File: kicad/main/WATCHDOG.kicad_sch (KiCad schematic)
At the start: 3 parts, among them U2 TPS3828-33DBVR

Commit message: Second review round
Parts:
- removed R135: 100k, Resistor_SMD:R_0603_1608Metric, symbol Device:R_US
- removed U2: TPS3828-33DBVR, JLCImport:TPS3828-33DBVR, symbol JLCImport:TPS3828-33DBVR
- added U3: STWD100NYWY3F, JLCImport:STWD100NYWY3F, symbol JLCImport:STWD100NYWY3F
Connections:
- net GND: now also U3.2 (GND)
- net VCC-3V3-P: now also U3.5 (VCC)
- net WDI: now also U3.4 (WDI)
- net ~{PULSE_OUT}: now also U3.1 (WDO)
- new net ~{EN}: U3.3 (EN)

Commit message: STM32 power rail switch
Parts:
- C56: value 100nF/50V -> 100nF/6.3V; LCSC C1591 -> C5356672
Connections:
- net VCC-3V3-P renamed VCC-3V3
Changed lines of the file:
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@@
 	(generator_version "10.0")
 	(paper "A2")
-	(junction
-		(at 271.78 194.31)
-		(diameter 0)
-		(color 0 0 0 0)
-	)
 	(wire
 		(pts
@@
 			(width 0)
 			(type default)
+		)
+	)
+	(global_label "VCC-3V3"
+		(shape input)
+		(at 271.78 194.31 90)
+		(fields_autoplaced yes)
+		(effects
+			(font
+				(size 1.27 1.27)
+			)
+			(justify left)
+		)
+		(property "Intersheetrefs" "${INTERSHEET_REFS}"
+			(at 271.78 182.6162 90)
+			(hide yes)
+			(show_name no)
+			(do_not_autoplace no)
+			(effects
+				(font
+					(size 1.27 1.27)
+				)
+				(justify left)
+			)
 		)
 	)
@@
 			)
 			(justify left)
-		)
-	)
-	(symbol
-		(lib_id "oomwoo-kicad-altium-import:VCC-3V3-P_BAR")
-		(at 271.78 194.31 180)
-		(unit 1)
-		(body_style 1)
-		(exclude_from_sim no)
-		(in_bom yes)
-		(on_board yes)
-		(in_pos_files yes)
-		(dnp no)
-		(property "Reference" "#PWR070"
-			(at 271.78 194.31 0)
-			(hide yes)
-			(show_name no)
-			(do_not_autoplace no)
-			(effects
-				(font
-					(size 1.27 1.27)
-				)
-			)
-		)
-		(property "Value" "VCC-3V3-P"
-			(at 271.78 190.5 0)
-			(show_name no)
-			(do_not_autoplace no)
-			(effects
-				(font
-					(size 1.27 1.27)
-				)
-			)
-		)
-		(property "Footprint" ""
-			(at 271.78 194.31 0)
-			(show_name no)
-			(do_not_autoplace no)
-			(effects
-				(font
-					(size 1.27 1.27)
-				)
-			)
-		)
-		(property "Datasheet" ""
-			(at 271.78 194.31 0)
-			(show_name no)
-			(do_not_autoplace no)
-			(effects
-				(font
-					(size 1.27 1.27)
-				)
-			)
-		)
-		(property "Description" ""
-			(at 271.78 194.31 0)
-			(show_name no)
-			(do_not_autoplace no)
-			(effects
-				(font
-					(size 1.27 1.27)
-				)
-			)
-		)
-		(pin ""
-		)
-		(instances
-			(project "Main"
-				(path "/dbcfb655-8d45-4808-9a74-2a0eb03372e8/7f043eef-851b-4fc7-bc1b-c170004bfbd9"
-					(reference "#PWR070")
-					(unit 1)
-				)
-			)
 		)
 	)
@@
 			)
 		)
-		(property "Value" "100nF/50V"
+		(property "Value" "100nF/6.3V"
 			(at 274.701 218.313 0)
 			(show_name no)
@@
 			)
 		)
-		(property "LCSC" "C1591"
+		(property "LCSC" "C5356672"
+			(at 271.78 217.17 0)
+			(hide yes)
+			(show_name no)
+			(do_not_autoplace no)
+			(effects
+				(font
+					(size 1.27 1.27)
+				)
+			)
+		)
+		(property "Arrow Part Number" ""
+			(at 271.78 217.17 0)
+			(hide yes)
+			(show_name no)
+			(do_not_autoplace no)
+			(effects
+				(font
+					(size 1.27 1.27)
+				)
+			)
+		)
+		(property "Arrow Price/Stock" ""
+			(at 271.78 217.17 0)
+			(hide yes)
+			(show_name no)
+			(do_not_autoplace no)
+			(effects
+				(font
+					(size 1.27 1.27)
+				)
+			)
+		)
+		(property "Comment" ""
+			(at 271.78 217.17 0)
+			(hide yes)
+			(show_name no)
+			(do_not_autoplace no)
+			(effects
+				(font
+					(size 1.27 1.27)
+				)
+			)
+		)
+		(property "Height" ""
+			(at 271.78 217.17 0)
+			(hide yes)
+			(show_name no)
+			(do_not_autoplace no)
+			(effects
+				(font
+					(size 1.27 1.27)
+				)
+			)
+		)
+		(property "Manufacturer_Name" ""
+			(at 271.78 217.17 0)
+			(hide yes)
+			(show_name no)
+			(do_not_autoplace no)
+			(effects
+				(font
+					(size 1.27 1.27)
+				)
+			)
+		)
+		(property "Mouser Part Number" ""
+			(at 271.78 217.17 0)
+			(hide yes)
+			(show_name no)
+			(do_not_autoplace no)
+			(effects
+				(font
+					(size 1.27 1.27)
+				)
+			)
+		)
+		(property "Mouser Price/Stock" ""
 			(at 271.78 217.17 0)
 			(hide yes)
@@
 			(at 292.1 196.85 0)
 			(hide yes)
+			(show_name no)
+			(do_not_autoplace no)
+			(effects
+				(font
+					(size 1.27 1.27)
+				)
+			)
+		)
+		(property "Arrow Part Number" ""
+			(at 292.1 196.85 0)
+			(hide yes)
+			(show_name no)
+			(do_not_autoplace no)
+			(effects
+				(font
+					(size 1.27 1.27)
+				)
+			)
+		)
+		(property "Arrow Price/Stock" ""
+			(at 292.1 196.85 0)
+			(hide yes)
+			(show_name no)
+			(do_not_autoplace no)
+			(effects
+				(font
+					(size 1.27 1.27)
+				)
+			)
+		)
+		(property "Comment" ""
+			(at 292.1 196.85 0)
+			(hide yes)
+			(show_name no)
+			(do_not_autoplace no)
+			(effects
+				(font
+					(size 1.27 1.27)
+				)
+			)
+		)
+		(property "Height" ""
+			(at 292.1 196.85 0)
+			(hide yes)
+			(show_name no)
+			(do_not_autoplace no)
+			(effects
+				(font
+					(size 1.27 1.27)
+				)
+			)
+		)
+		(property "Manufacturer_Name" ""
+			(at 292.1 196.85 0)
+			(hide yes)
+			(show_name no)
+			(do_not_autoplace no)
+			(effects
+				(font
+					(size 1.27 1.27)
+				)
+			)
+		)
+		(property "Mouser Part Number" ""
+			(at 292.1 196.85 0)
+			(hide yes)
+			(show_name no)
+			(do_not_autoplace no)
+			(effects
+				(font
+					(size 1.27 1.27)
+				)
+			)
+		)
+		(property "Mouser Price/Stock" ""
+			(at 292.1 196.85 0)
+			(hide yes)

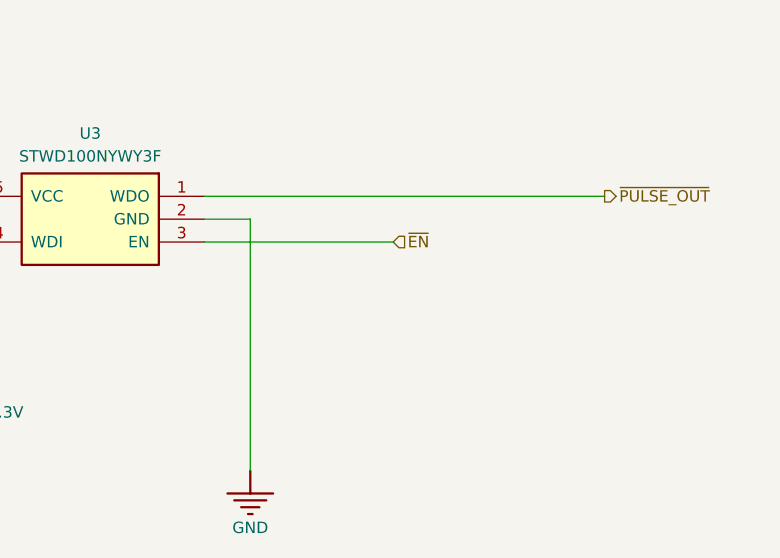
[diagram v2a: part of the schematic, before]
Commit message: Update Power Control sch, Charger sch, Speaker + Mic, JTAG and Watch Dog
**Power Control:** Replaced the BJT with a MOSFET. The MCU hang condition is not covered yet.
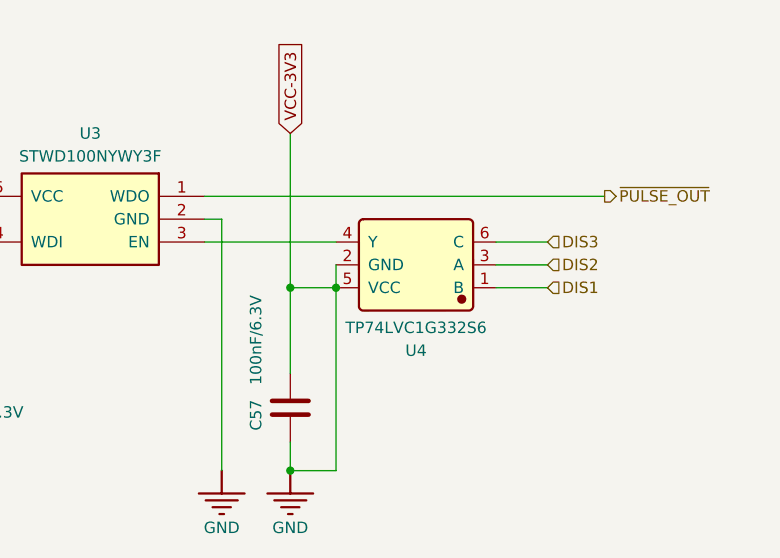
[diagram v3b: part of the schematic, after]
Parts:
- added C57: 100nF/6.3V, Capacitor_SMD:C_0603_1608Metric, symbol Device:C
- added U4: TP74LVC1G332S6, JLCImport:TP74LVC1G332S6, symbol JLCImport:TP74LVC1G332S6
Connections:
- net VCC-3V3 is gone; now on net GND: C56.1, U3.5 (VCC)
- net GND: now also C57.1, C57.2, U4.2 (GND), U4.5 (VCC)
- net ~{EN}: no longer names the net of U3.3 (EN)
- net ~{EN}: now also U4.4 (Y)
- new net DIS1: U4.1 (B)
- new net DIS2: U4.3 (A)
- new net DIS3: U4.6 (C)

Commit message: Claude added RC watchdog
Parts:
- added C7001: 100nF/6.3V, Capacitor_SMD:C_0603_1608Metric, symbol Device:C
- added C7002: 10uF/6.3V, Capacitor_SMD:C_0603_1608Metric, symbol Device:C
- added Q7001: WG3401, JLCImport:WG3401, symbol JLCImport:WG3401
- added R7001, R7003: 1k, Resistor_SMD:R_0603_1608Metric, symbol Device:R_US
- added R7002: 100k, Resistor_SMD:R_0603_1608Metric, symbol Device:R_US
- added R7004: 10k, Resistor_SMD:R_0603_1608Metric, symbol Device:R_US
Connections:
- net GND: now also C7002.2, R7004.2; no longer C56.1, C57.1, U3.5 (VCC), U4.5 (VCC)
- net WDI: now also R7001.1
- new net: C7001.2, Q7001.1 (G), R7002.2
- new net: Q7001.3 (D), R7003.1
- new net: C7001.1, R7001.2
- new net VCC-3V3: C56.1, C57.1, Q7001.2 (S), R7002.1, U3.5 (VCC), U4.5 (VCC)
- new net WD_OK: C7002.1, R7003.2, R7004.1
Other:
- note added: "Firmware toggles WDI in software (50-1000 Hz, ~50% duty) only while the control loop is healthy. Never drive WDI from a timer/PWM: a timer keeps running after the CPU hangs. Each falling edge on WDI pulls the Q7001 gate low through C7001 and tops up C7002 via R7003. WD_OK ~2.7 V while toggling. WDI stuck high, low or floating: <1 V in ~100 ms, <0.4 V in ~190 ms (10 uF nominal; DC-bias derating sh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"
- note added: "RC CHARGE-PUMP WATCHDOG (motor power only; output not wired yet)"

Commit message: Cleaned up schematic filenames
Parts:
- Q7001: value WG3401 -> AO3401; footprint JLCImport:WG3401 -> JLCImport:AO3401; symbol JLCImport:WG3401 -> JLCImport:AO3401; LCSC C7541474 -> C20628875; Manufacturer (none) -> FOSAN; Manufacturer Part (none) -> AO3401
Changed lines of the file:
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@@
+		)
+	)
+	(global_label "WD_OK"
+		(shape output)
+		(at 322.58 288.29 0)
+		(fields_autoplaced yes)
+		(effects
+			(font
+				(size 1.27 1.27)
+			)
+			(justify left)
+		)
+		(property "Intersheetrefs" "${INTERSHEET_REFS}"
+			(at 322.58 288.29 0)
+			(hide yes)
+			(show_name no)
+			(do_not_autoplace no)
+			(effects
+				(font
+					(size 1.27 1.27)
+				)
+				(justify left)
+			)
 		)
 	)
@@
 		(shape output)
 		(at 349.25 194.31 0)
-		(effects
-			(font
-				(size 1.27 1.27)
-			)
-			(justify left)
-		)
-	)
-	(hierarchical_label "WD_OK"
-		(shape output)
-		(at 322.58 288.29 0)
 		(effects
 			(font
@@
 	)
 	(symbol
-		(lib_id "JLCImport:WG3401")
+		(lib_id "JLCImport:AO3401")
 		(at 292.1 270.51 0)
 		(mirror x)
@@
 			)
 		)
-		(property "Value" "WG3401"
+		(property "Value" "AO3401"
 			(at 298.45 272.415 0)
 			(show_name no)
@@
 			)
 		)
-		(property "Footprint" "JLCImport:WG3401"
+		(property "Footprint" "JLCImport:AO3401"
 			(at 292.1 270.51 0)
 			(hide yes)
@@
 			)
 		)
-		(property "Datasheet" "https://wmsc.lcsc.com/wmsc/upload/file/pdf/v2/lcsc/2310101751_Wild-Goose-WG3401_C7541474.pdf"
+		(property "Datasheet" "https://wmsc.lcsc.com/wmsc/upload/file/pdf/v2/lcsc/2403011756_FOSAN-AO3401_C20628875.pdf"
 			(at 292.1 270.51 0)
 			(hide yes)
@@
 			)
 		)
-		(property "Description" "P-FET pump switch"
+		(property "Description" "-30V -4.4A P-channel MOSFET, 52mOhm@-4.5V, Vgs +/-12V, SOT-23"
 			(at 292.1 270.51 0)
 			(hide yes)
@@
 			)
 		)
-		(property "LCSC" "C7541474"
+		(property "LCSC" "C20628875"
 			(at 292.1 270.51 0)
 			(hide yes)
+			(show_name no)
+			(do_not_autoplace no)
+			(effects
+				(font
+					(size 1.27 1.27)
+				)
+			)
+		)
+		(property "Manufacturer" "FOSAN"
+			(at 292.1 270.51 0)
+			(hide yes)
+			(show_name no)
+			(do_not_autoplace no)
+			(effects
+				(font
+					(size 1.27 1.27)
+				)
+			)
+		)
+		(property "Manufacturer Part" "AO3401"
+			(at 292.1 270.51 0)
+			(hide yes)

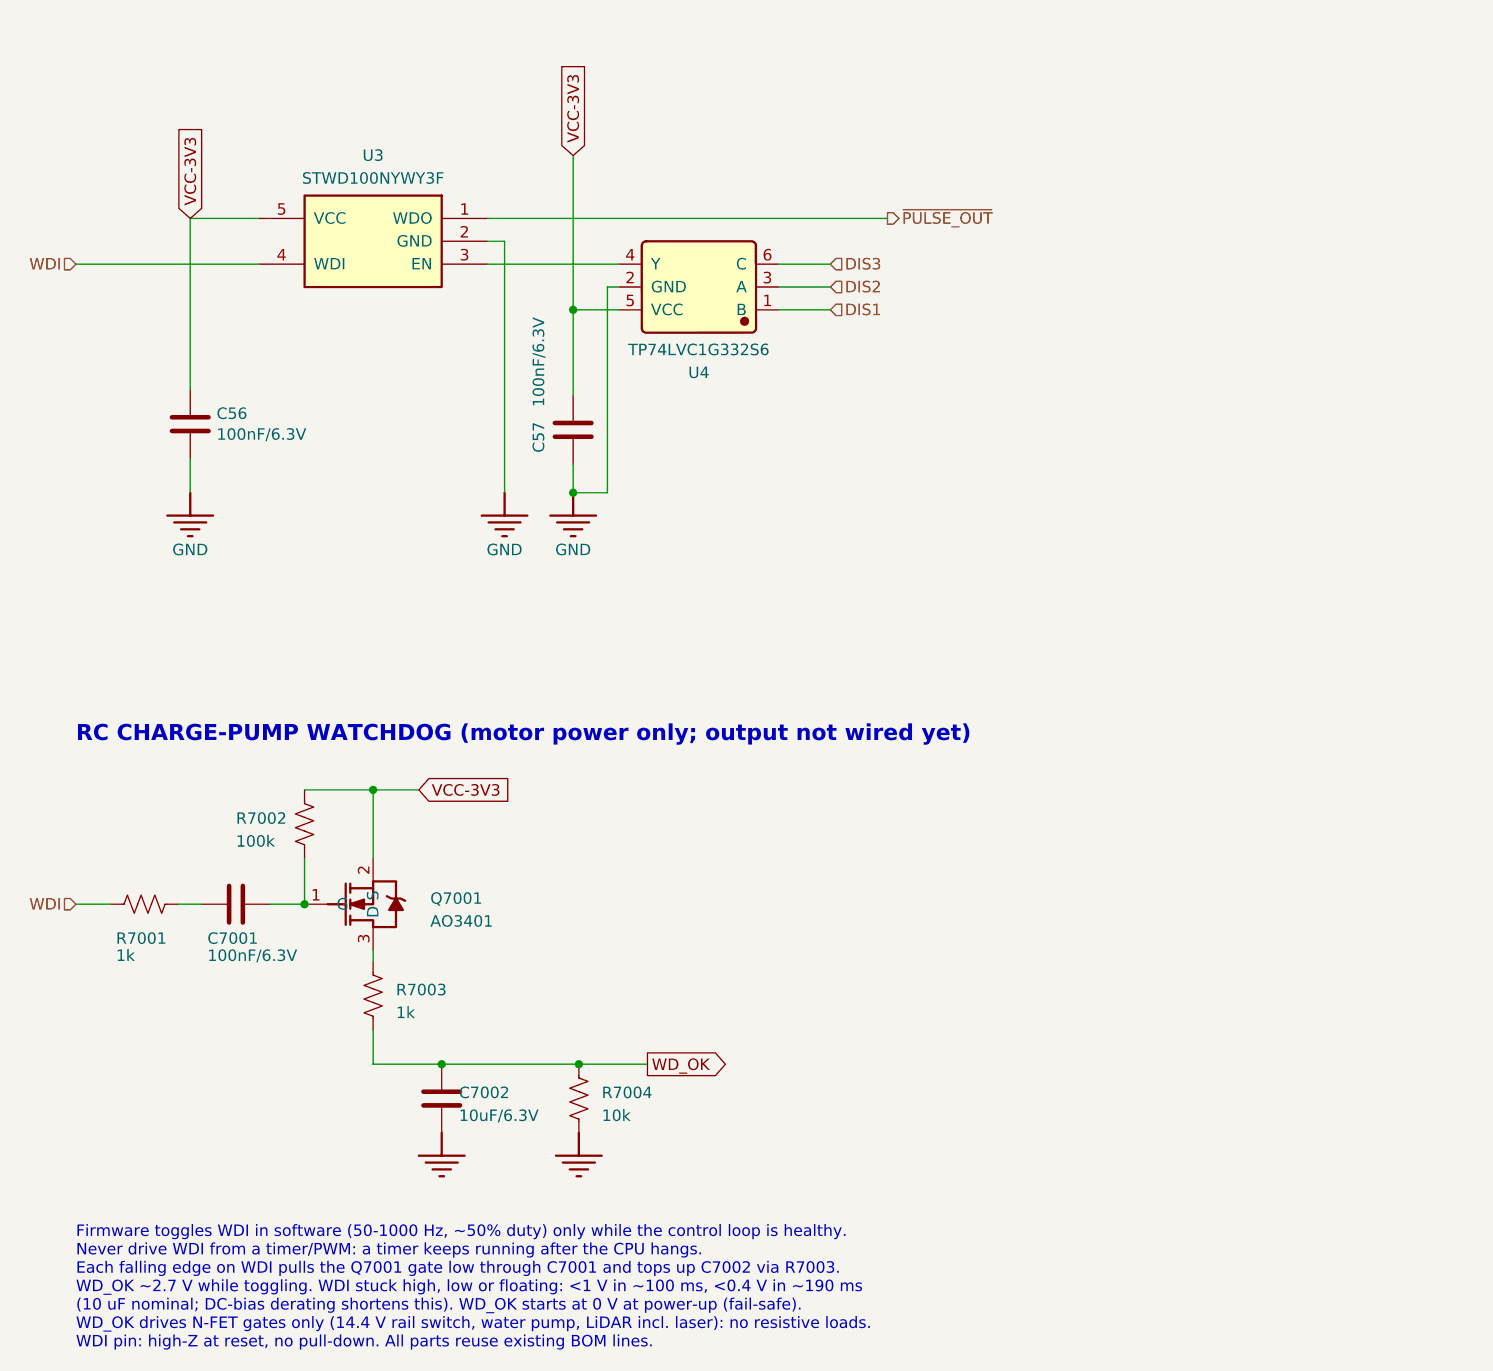
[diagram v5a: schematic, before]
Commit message: Cleanup; renamed WDO to WDI
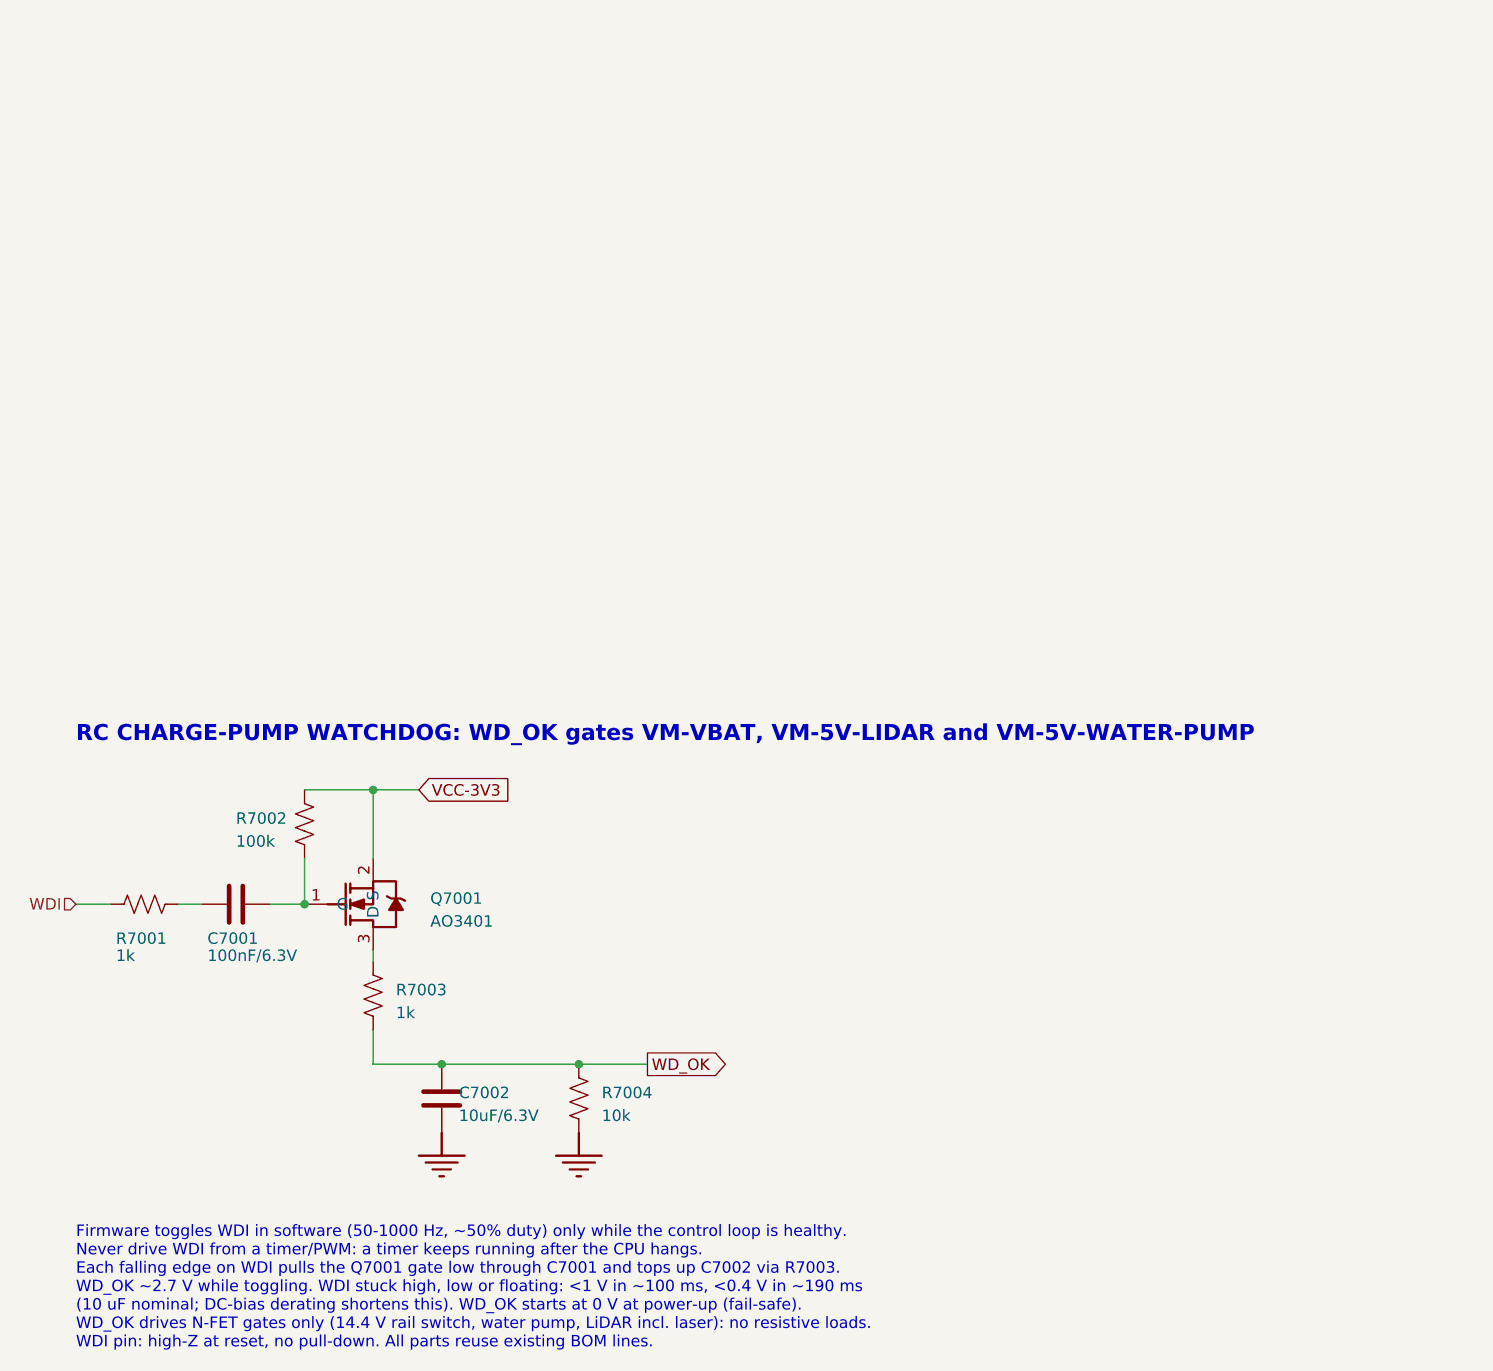
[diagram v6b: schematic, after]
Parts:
- removed C56, C57: 100nF/6.3V, Capacitor_SMD:C_0603_1608Metric, symbol Device:C
- removed U3: STWD100NYWY3F, JLCImport:STWD100NYWY3F, symbol JLCImport:STWD100NYWY3F
- removed U4: TP74LVC1G332S6, JLCImport:TP74LVC1G332S6, symbol JLCImport:TP74LVC1G332S6
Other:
- note added: "RC CHARGE-PUMP WATCHDOG: WD_OK gates VM-VBAT, VM-5V-LIDAR and VM-5V-WATER-PUMP"
- note removed: "RC CHARGE-PUMP WATCHDOG (motor power only; output not wired yet)"
